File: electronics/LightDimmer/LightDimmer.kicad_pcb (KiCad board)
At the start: 2 copper layers, 53.5 x 57.5 mm, 11 parts, among them J1 Serial Terminals, J2 AC Terminals, U1 ESP-12F, U2 5V07, U3 AC Dimmer 4A

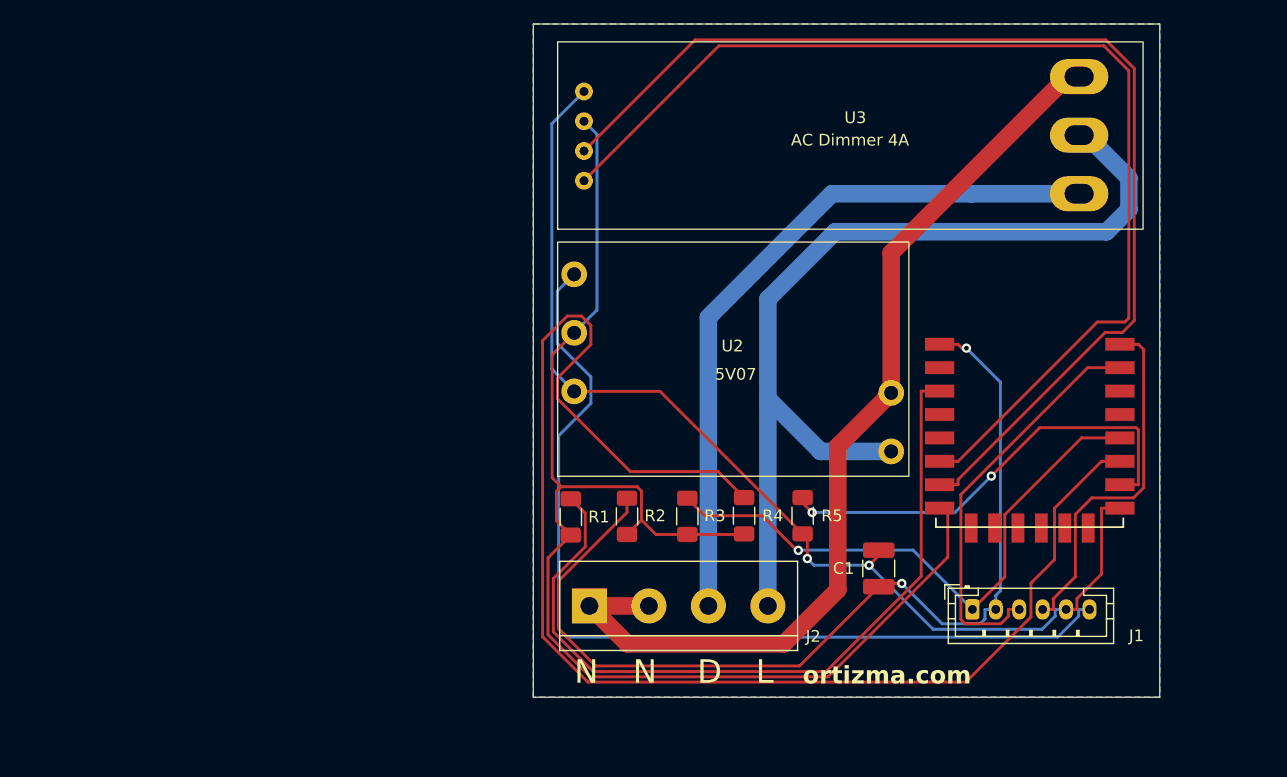
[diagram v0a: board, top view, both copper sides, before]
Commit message: Improve file naming & Design V2 Dimmer iteration & Lay components in PCB
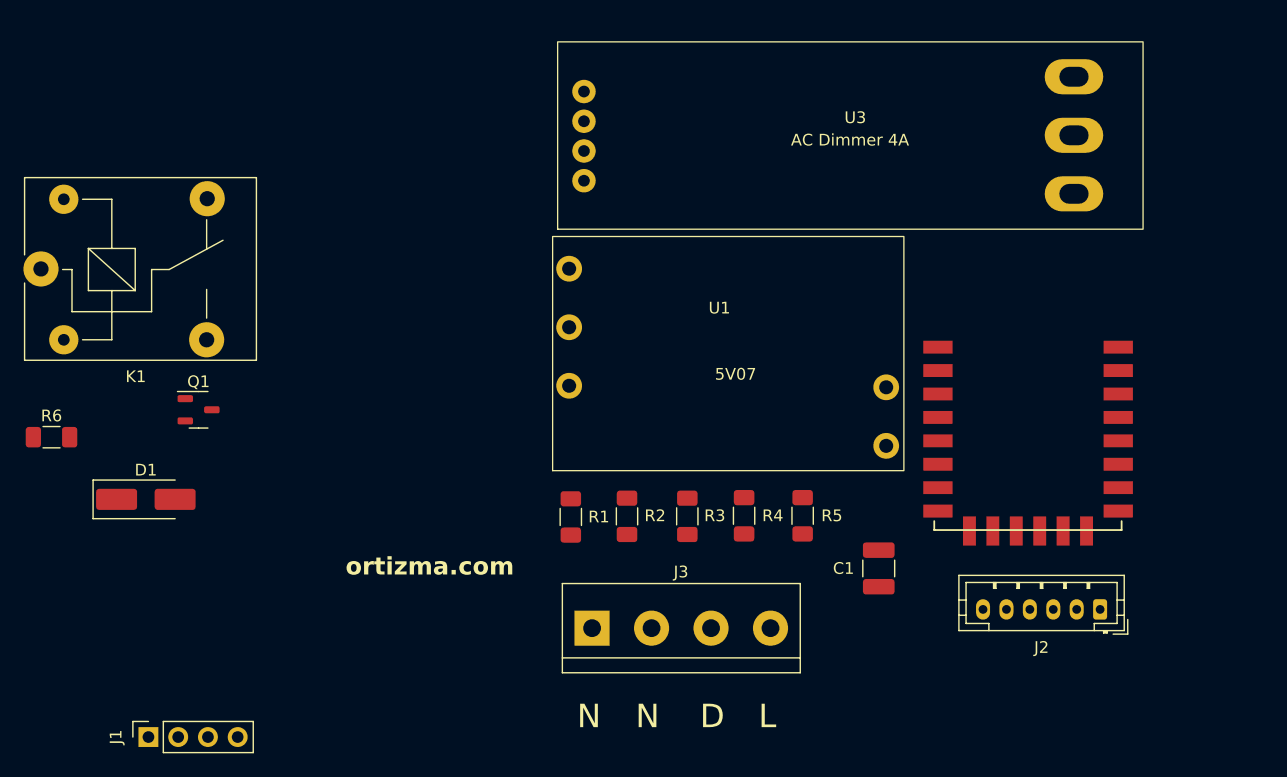
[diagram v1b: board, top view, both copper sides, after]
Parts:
- added D1: 1N4007, Diode_SMD:D_SMA_Handsoldering, F.Cu at (88.9, 111.8)
- added J3: AC Terminals, AA_Footprints:Terminal_KF128-4P, F.Cu at (127.0, 122.8)
- added K1: SANYOU_SRD_Form_C, Relay_THT:Relay_SPDT_SANYOU_SRD_Series_Form_C, F.Cu at (79.9, 92.2)
- added Q1: BC547, AA_Footprints:SOT-23-3-BC, F.Cu at (93.4, 104.2)
- added R6: 1k, Resistor_SMD:R_1206_3216Metric_Pad1.30x1.75mm_HandSolder, F.Cu at (80.8, 106.5)
- J1: value Serial Terminals -> 433MHz_ASK_Superheterodyne_Receiver; footprint Connector_JST:JST_PH_B6B-PH-K_1x06_P2.00mm_Vertical -> AA_Footprints:RF Receiver
- J2: value AC Terminals -> Serial Terminals; footprint TerminalBlock:TerminalBlock_bornier-4_P5.08mm -> Connector_JST:JST_PH_B6B-PH-K_1x06_P2.00mm_Vertical
- U1: value ESP-12F -> 5V07 Transformer; footprint AA_Footprints:ESP-12E_SMD -> AA_Footprints:5V07
- U2: value 5V07 -> ESP-12F; footprint AA_Footprints:5V07 -> AA_Footprints:ESP-12E_SMD
- U3: value AC Dimmer 4A -> AC_Dimmer_4A
- moved J1 71.2 mm to (89.1, 132.2), turned to 90 degrees
- moved J2 43.6 mm to (170.4, 121.2), turned to 180 degrees
- moved U1 19.2 mm to (138.2, 99.6)
- moved U2 18.7 mm to (157.2, 98.8)
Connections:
- J1 pad 1: /GPIO0 -> GND
- J1 pad 2: /REST -> /GPIO14
- J1 pad 3: /RX -> /GPIO14
- J1 pad 4: /TX -> +3.3V
- J2 pad 1: NEUT -> /GPIO0
- J2 pad 2: NEUT -> /REST
- J2 pad 3: LAMP -> /RX
- J2 pad 4: AC -> /TX
- U1 pad 1: /REST -> LINE
- U1 pad 2: /ADC -> NEUT
- U1 pad 3: /EN -> GND
- U1 pad 4: /GPIO16 -> +3.3V
- U1 pad 5: /GPIO14 -> +5V
- U2 pad 1: AC -> /REST
- U2 pad 2: NEUT -> /ADC
- U2 pad 3: GND -> /EN
- U2 pad 4: +3.3V -> /GPIO16
- U2 pad 5: +5V -> /GPIO14
- U3 pad 6: AC -> LINE
- U3 pad 7: LAMP -> DIMMER_OUT
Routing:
- net /GPIO2: track 119.8 -> 0.00 mm
- net +3.3V: track 112.3 -> 0.00 mm
- net /GPIO13: track 95.5 -> 0.00 mm
- net /GPIO12: track 93.8 -> 0.00 mm
- net GND: track 93.0 -> 0.00 mm, vias 2 -> 0
- net /REST: track 83.0 -> 0.00 mm, vias 2 -> 0
- net NEUT: track 82.5 -> 0.00 mm
- net AC: track 81.1 -> 0.00 mm
- net +5V: track 80.2 -> 0.00 mm
- net /EN: track 67.3 -> 0.00 mm
- net LAMP: track 60.7 -> 0.00 mm
- net /GPIO0: track 49.4 -> 0.00 mm, vias 1 -> 0
- net /GPIO15: track 39.5 -> 0.00 mm, vias 2 -> 0
- net /RX: track 34.0 -> 0.00 mm
- net /TX: track 31.3 -> 0.00 mm
- removed copper zone on B.Cu, net GND
- removed copper zone on F.Cu, net GND
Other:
- board outline removed

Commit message: Finish LightDimmer PCB Design V2
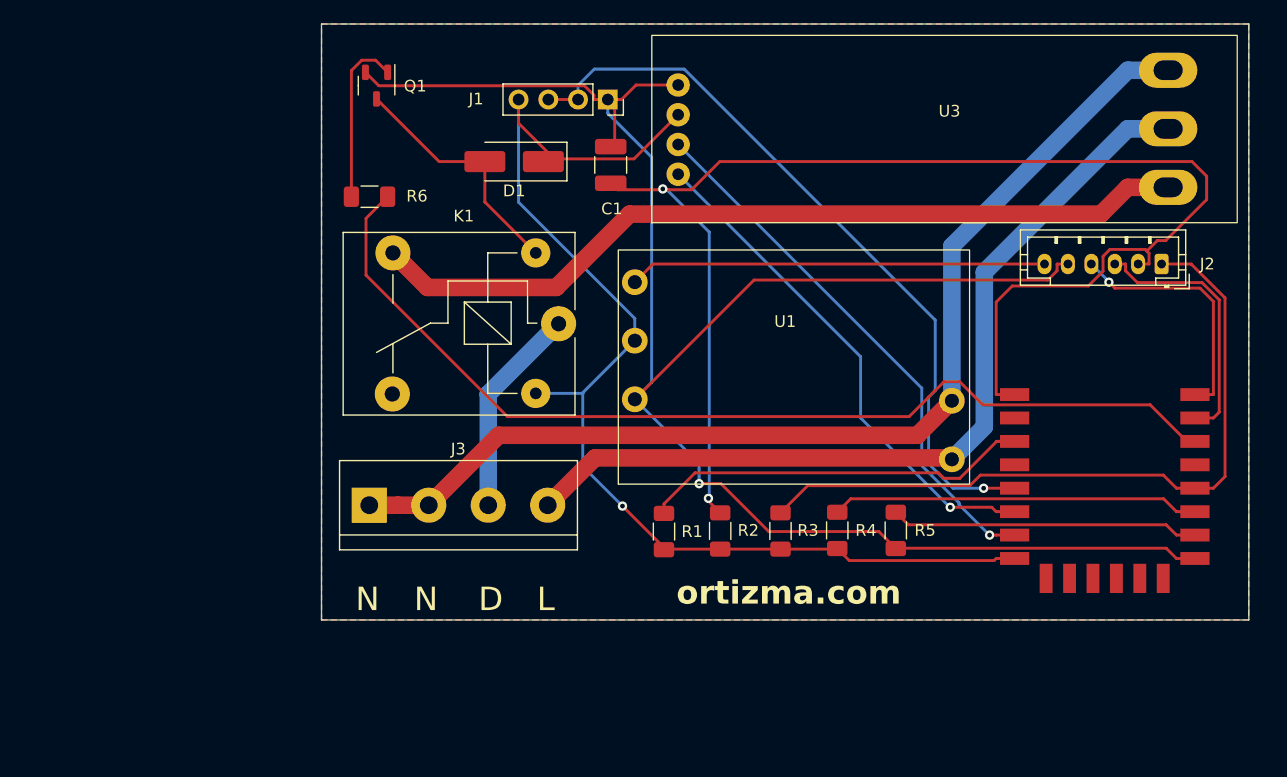
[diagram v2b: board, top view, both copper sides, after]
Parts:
- moved J1 67.1 mm to (128.3, 77.7), turned to -90 degrees
- moved K1 44.5 mm to (124.2, 96.8), turned to 180 degrees
- moved D1 42.7 mm to (120.3, 83.0), turned to 180 degrees
- moved C1 41.4 mm to (128.6, 83.3)
- moved R6 34.1 mm to (108.0, 86.0), turned to 180 degrees
- moved Q1 31.6 mm to (108.6, 76.5), turned to -90 degrees
- moved J2 30.0 mm to (175.7, 91.8)
- moved J3 21.7 mm to (108.0, 112.3)
- moved U3 8.06 mm to (157.5, 80.2)
- moved R1 8.05 mm to (133.2, 114.6)
- moved R3 8.05 mm to (143.1, 114.5)
- moved R2 8.05 mm to (137.9, 114.5)
- moved R4 8.05 mm to (147.9, 114.5)
- moved R5 8.05 mm to (152.9, 114.5)
- moved U2 7.70 mm to (163.8, 102.9)
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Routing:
- net GND: track 0.00 -> 156.2 mm, vias 0 -> 1
- net /REST: track 0.00 -> 119.8 mm, vias 0 -> 2
- net +3.3V: track 0.00 -> 101.8 mm, vias 0 -> 1
- net NEUT: track 0.00 -> 91.4 mm
- net /GPIO5: track 0.00 -> 85.9 mm
- net LINE: track 0.00 -> 74.1 mm
- net DIMMER_OUT: track 0.00 -> 71.0 mm
- net /GPIO14: track 0.00 -> 65.1 mm, vias 0 -> 1
- net /GPIO0: track 0.00 -> 62.1 mm
- net /GPIO13: track 0.00 -> 47.2 mm, vias 0 -> 1
- net /GPIO12: track 0.00 -> 44.4 mm, vias 0 -> 1
- net /EN: track 0.00 -> 36.3 mm
- net +5V: track 0.00 -> 35.6 mm
- net /GPIO2: track 0.00 -> 30.8 mm
- net /GPIO15: track 0.00 -> 25.7 mm
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- added copper zone on B.Cu, net GND
- added copper zone on F.Cu, net GND
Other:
- board outline added: 79.2 x 50.9 mm
- board text removed: "5V07"
- board text removed: "AC Dimmer 4A"

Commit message: Improved the designs of LightController & LightDimmer PCBs
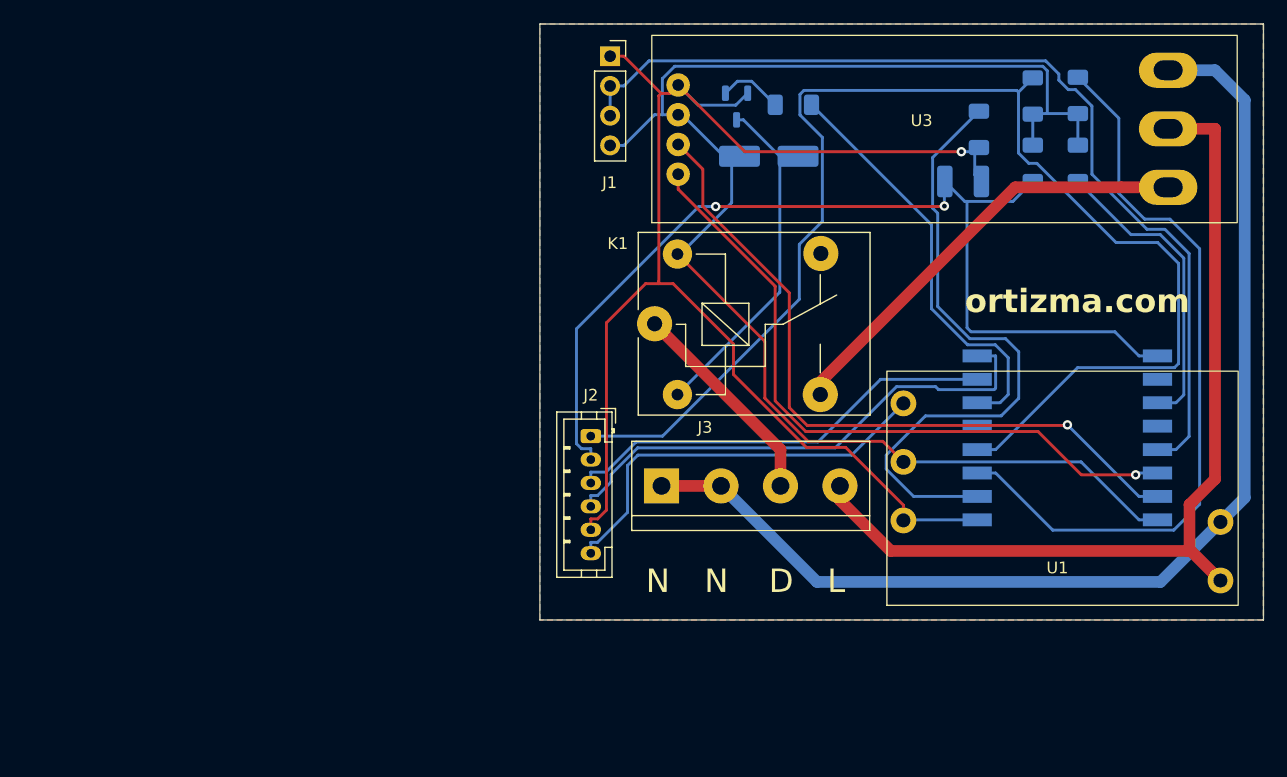
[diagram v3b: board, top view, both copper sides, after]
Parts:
- C1, D1, Q1, R1, R2, R3, R4, R5, R6: moved to B.Cu
- U2: footprint AA_Footprints:ESP-12E_SMD -> AA_Footprints:ESP-12E_SMD_Simple; moved to B.Cu
- moved J2 50.9 mm to (126.9, 106.5), turned to -90 degrees
- moved R1 47.3 mm to (168.5, 83.2), turned to -90 degrees
- moved R3 42.9 mm to (164.7, 77.4)
- moved R4 42.5 mm to (168.5, 77.3)
- moved R2 41.2 mm to (164.7, 83.2), turned to -90 degrees
- moved R6 37.0 mm to (144.2, 78.2)
- moved R5 35.0 mm to (160.1, 80.2)
- moved Q1 30.8 mm to (139.3, 78.3)
- moved C1 30.1 mm to (158.7, 84.7), turned to 0 degrees
- moved U1 25.2 mm to (166.8, 111.1)
- moved J3 25.0 mm to (132.9, 110.7)
- moved D1 21.8 mm to (142.1, 82.5), turned to 0 degrees
- moved U2 11.3 mm to (174.6, 99.6), turned to 180 degrees
- moved K1 8.20 mm to (132.3, 96.8), turned to 0 degrees
- moved J1 3.71 mm to (128.6, 74.0), turned to 0 degrees
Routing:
- net /GPIO0: track 62.1 -> 113.2 mm
- net /GPIO5: track 85.9 -> 35.3 mm
- net /REST: track 119.8 -> 86.3 mm
- net DIMMER_OUT: track 71.0 -> 37.7 mm
- net /GPIO2: track 30.8 -> 63.3 mm
- net GND: track 156.2 -> 125.0 mm
- net /GPIO15: track 25.7 -> 54.9 mm
- net +3.3V: track 101.8 -> 125.9 mm, vias 1 -> 0
- net /TX: track 22.0 -> 43.5 mm, vias 1 -> 0
- net /GPIO14: track 65.1 -> 82.9 mm, vias 1 -> 0
- net /RX: track 23.1 -> 37.9 mm
- net /GPIO13: track 47.2 -> 60.3 mm
- net /GPIO12: track 44.4 -> 57.4 mm
- net /EN: track 36.3 -> 26.7 mm
- net Net-(D1-A): track 21.1 -> 30.5 mm
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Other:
- board size 79.2 x 50.9 mm -> 61.8 x 50.9 mm
